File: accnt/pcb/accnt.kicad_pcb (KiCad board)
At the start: 2 copper layers, 19.7 x 23 mm, 18 parts, among them J1 Conn_ARM_JTAG_SWD_10, J2 Conn_01x04_Male, Q1 2N7002E, Q2 2N7002E, U1 Holyiot-18010, U2 MIC5365-3.3YD5

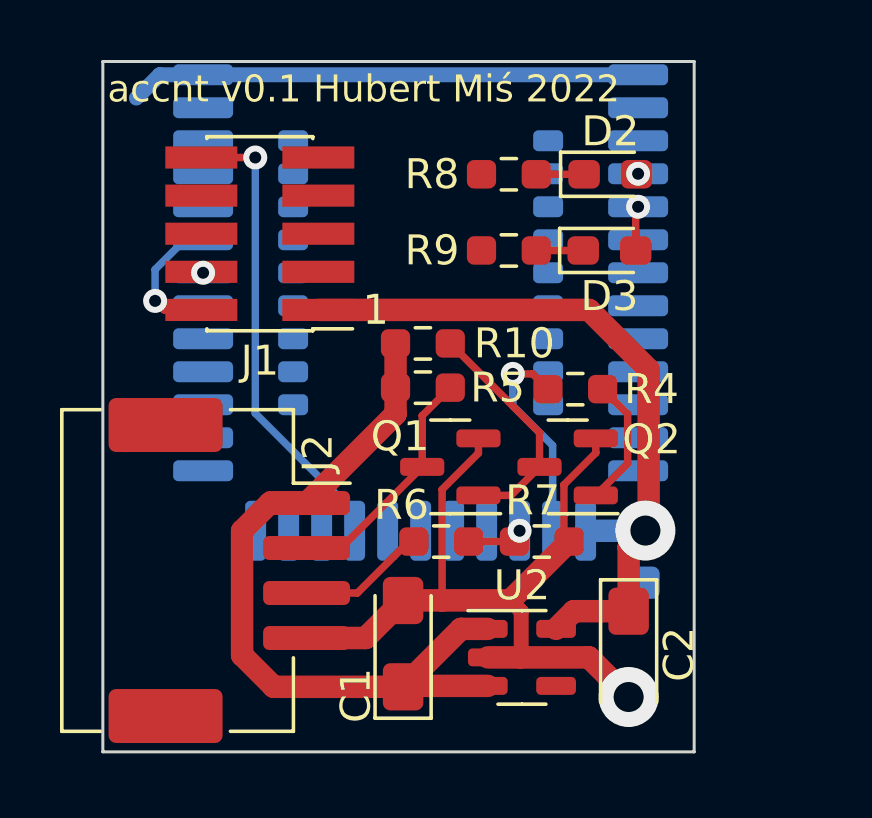
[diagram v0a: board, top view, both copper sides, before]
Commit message: accnt: fix missing GND connection in PCB
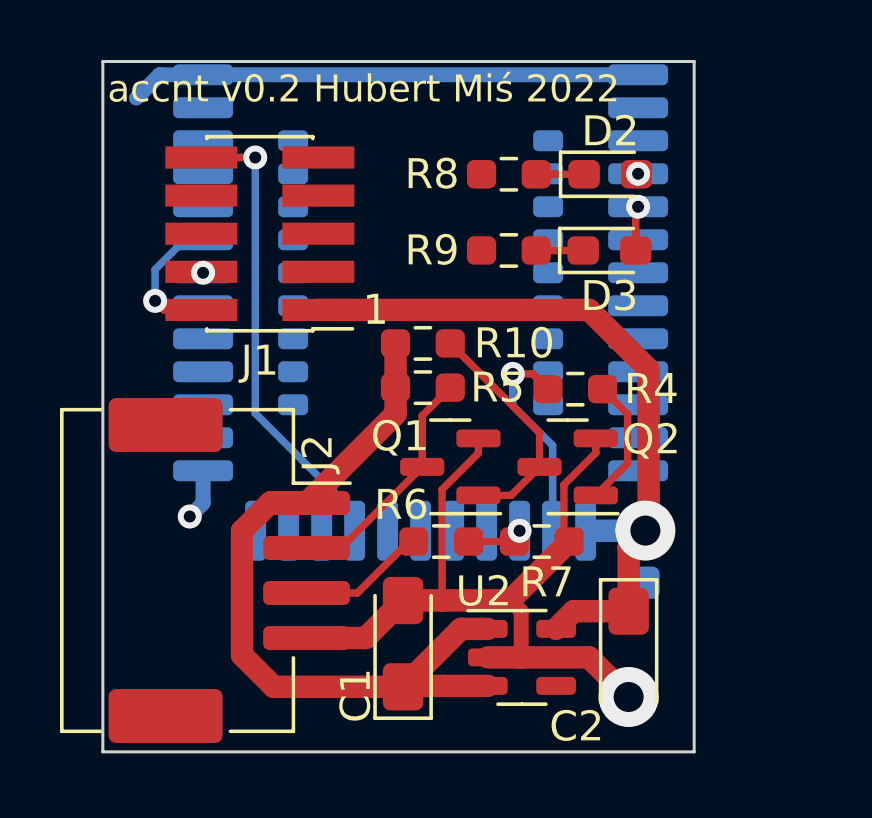
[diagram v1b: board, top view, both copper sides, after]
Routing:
- net GND: track 44.3 -> 46.0 mm, vias 1 -> 2
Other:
- board text added: "accnt v0.2 Hubert Miś 2022"
- board text removed: "accnt v0.1 Hubert Miś 2022"
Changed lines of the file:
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@@
     (property "Sheetname" "")
     (attr smd)
-    (fp_text reference "U2" (at 0 -2.4) (layer "F.SilkS")
+    (fp_text reference "U2" (at -1.2736 -2.1956) (layer "F.SilkS")
       (effects (font (size 1 1) (thickness 0.15)))
     )
@@
     (property "Sheetname" "")
     (attr smd)
-    (fp_text reference "C2" (at 0 -1.6764 90) (layer "F.SilkS")
+    (fp_text reference "C2" (at 2.406 1.7296 180) (layer "F.SilkS")
       (effects (font (size 1 1) (thickness 0.15)))
     )
@@
     (property "Sheetname" "")
     (attr smd)
-    (fp_text reference "R7" (at -0.3048 -1.3716) (layer "F.SilkS")
+    (fp_text reference "R7" (at 0.166 1.3652) (layer "F.SilkS")
       (effects (font (size 1 1) (thickness 0.15)))
     )
@@
   )
   (gr_rect (start 54.2036 46.5328) (end 73.914 69.5452) (layer "Edge.Cuts") (width 0.1) (fill none))
-  (gr_text "accnt v0.1 Hubert Miś 2022" (at 54.356 47.4472) (layer "F.SilkS")
+  (gr_text "accnt v0.2 Hubert Miś 2022" (at 54.356 47.4472) (layer "F.SilkS")
     (effects (font (size 0.9 0.9) (thickness 0.15)) (justify left))
   )
@@
   (segment (start 68.1228 66.3956) (end 70.4088 66.3956) (width 0.75) (layer "F.Cu") (net 2))
   (segment (start 69.7465 62.5348) (end 69.57308 62.36138) (width 0.25) (layer "F.Cu") (net 2))
+  (via (at 57.1 61.7) (size 0.8) (drill 0.4) (layers "F.Cu" "B.Cu") (net 2))
   (via (at 71.7296 67.7164) (size 2) (drill 1) (layers "F.Cu" "B.Cu") (net 2))
+  (segment (start 57.545 61.255) (end 57.1 61.7) (width 0.5) (layer "B.Cu") (net 2))
+  (segment (start 57.545 60.175) (end 57.545 61.255) (width 0.5) (layer "B.Cu") (net 2))
   (segment (start 72.045 46.975) (end 57.545 46.975) (width 0.5) (layer "B.Cu") (net 2))
   (segment (start 56.0982 46.975) (end 55.3212 47.752) (width 0.5) (layer "B.Cu") (net 2))
